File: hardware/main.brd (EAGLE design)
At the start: 99 x 99 mm, 37 parts, among them U1 TMS320F28069_PN_80, U10 TXB0101_DBV_6, U2 TXB0101_DBV_6, U3 TS3A5018_PW_16, U4 TS3A5018_PW_16, U5 SN74LVC4245A_DW_24, U7 Value, U8 Value, U9 SN74LVC4245A_DW_24

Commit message: Finished schematic, laid out board
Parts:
- removed EXTCON2: M10SILK_FEMALE_PTH, SparkFun-Connectors:1X10
- added JP3: M10SILK_FEMALE_PTH, SparkFun-Connectors:1X10
- added U$4, U$8: 8PIN_SOCKET, ControllerCard:CONN-8PIN
- moved C10 78.1 mm to (62.9, 23.6), flipped to the bottom
- moved C11 78.1 mm to (62.9, 19.8), flipped to the bottom
- moved C9 78.1 mm to (62.9, 27.4), flipped to the bottom
- moved C8 72.8 mm to (74.9, 19.3), flipped to the bottom
- moved C6 72.5 mm to (61.9, 10.9), flipped to the bottom
- moved R7 61.6 mm to (77.3, 29.2), turned to 180 degrees
- moved C7 56.5 mm to (52.9, 22.1), flipped to the bottom
- moved R5 55.2 mm to (69.2, 32.9), flipped to the bottom, turned to 270 degrees
- moved C5 49.6 mm to (87.3, 50.4)
- moved U$2 47.0 mm to (52.6, 8.54), turned to 90 degrees
- moved U$5 45.7 mm to (81.3, 51.2), turned to 0 degrees
- moved R2 44.4 mm to (45.4, 8.99)
- moved R3 43.2 mm to (43.7, 4.55), turned to 270 degrees
- moved R1 40.5 mm to (64.7, 3.17)
- moved EXTCON1 40.0 mm to (48.0, 44.4)
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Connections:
- removed net IBUFIN1: U7.23
- removed net IBUFIN2: U7.22
- removed net IBUFIN3: U7.20
- removed net IBUFIN4: U7.19
- removed net IBUFIN5: U7.18
- removed net IBUFIN6: U7.17
- removed net IBUFIN7: U7.15
- removed net IBUFIN8: U7.14
- removed net OBUFIN1: U8.1
- removed net OBUFIN2: U8.3
- removed net OBUFIN3: U8.4
- removed net OBUFIN4: U8.6
- removed net OBUFIN5: U8.7
- removed net OBUFIN6: U8.9
- removed net OBUFIN7: U8.10
- removed net OBUFIN8: U8.12
- new net N$13: U$4.P$1, U8.1
- new net N$14: U$4.P$2, U8.3
- new net N$15: U$4.P$3, U8.4
- new net N$16: U$4.P$4, U8.6
- new net N$17: U$4.P$8, U8.12
- new net N$18: U$4.P$7, U8.10
- new net N$19: U$4.P$6, U8.9
- new net N$20: U$4.P$5, U8.7
- new net N$21: U$8.P$1, U7.23
- new net N$22: U$8.P$2, U7.22
- new net N$23: U$8.P$3, U7.20
- new net N$24: U$8.P$4, U7.19
- new net N$25: U$8.P$8, U7.14
- new net N$26: U$8.P$7, U7.15
- new net N$27: U$8.P$6, U7.17
- new net N$28: U$8.P$5, U7.18
- net !FLASHEN!: now also U1.78; no longer U1.45
- net !FLASHHOLD!: now also U1.80; no longer U1.46
- net !FLASHWP!: now also U1.79; no longer U1.43
- net 3.3V: no longer EXTCON2.1
- net 5V: now also JP3.10
- net BIN1: no longer EXTCON1.4
- net BIN2: no longer EXTCON1.6
- net BIN3: no longer EXTCON1.8
- net BIN4: no longer EXTCON1.10
- net BIN5: no longer EXTCON1.14
- net BIN6: no longer EXTCON1.16
- net BIN7: no longer EXTCON1.18
- net BIN8: no longer EXTCON1.20
- net GND: now also JP3.1; no longer EXTCON2.10
- net IBUFOUT1: now also EXTCON1.4
- net IBUFOUT2: now also EXTCON1.6
- net IBUFOUT3: now also EXTCON1.8
- net IBUFOUT4: now also EXTCON1.10
- net IBUFOUT5: now also EXTCON1.14
- net IBUFOUT6: now also EXTCON1.16
- net IBUFOUT7: now also EXTCON1.18
- net IBUFOUT8: now also EXTCON1.20
- net N$10: now also JP3.8
- net N$11: now also JP3.7
- net N$12: now also JP3.6
- net N$5: now also JP3.2
- net N$6: now also JP3.3
- net N$7: now also JP3.4
- net N$8: now also JP3.5
- net N$9: now also JP3.9
- net SPICLK: now also U1.76; no longer U1.41
- net SPISIMO: now also U1.77; no longer U1.44
- net SPISOMI: now also U1.75; no longer U1.42
- net UCIN1: now also U1.31; no longer U1.8
- net UCIN2: now also U1.32; no longer U1.31
- net UCIN3: now also U1.33; no longer U1.32
- net UCIN4: now also U1.34; no longer U1.33
- net UCIN5: now also U1.35; no longer U1.34
- net UCIN6: now also U1.39; no longer U1.35
- net UCIN7: now also U1.40; no longer U1.39
- net UCIN8: now also U1.41; no longer U1.40
- net UCOUT1: now also U1.42; no longer EXTCON2.2, U1.66
- net UCOUT2: now also U1.43; no longer EXTCON2.3, U1.67
- net UCOUT3: now also U1.44; no longer EXTCON2.4, U1.68
- net UCOUT4: now also U1.45; no longer EXTCON2.5, U1.69
- net UCOUT5: now also U1.46; no longer EXTCON2.6, U1.70
- net UCOUT6: now also U1.52; no longer EXTCON2.7, U1.75
- net UCOUT7: now also U1.53; no longer EXTCON2.8, U1.76
- net UCOUT8: now also U1.59; no longer EXTCON2.9, U1.77
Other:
- board size 99 x 99 mm -> 91 x 58 mm

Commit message: Began routing
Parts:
- moved JP3 26.5 mm to (30.5, 30.5), turned to 180 degrees
- moved C2 14.1 mm to (46.4, 26.0), turned to 270 degrees
- moved EXTCON1 11.2 mm to (58.0, 49.4)
- moved U$3 10.8 mm to (49.6, 24.4), turned to 90 degrees
- moved C1 7.81 mm to (47.9, 18.9)
- moved C7 6.51 mm to (59.4, 21.9), turned to 270 degrees
- moved R1 6.00 mm to (62.3, 8.69), turned to 0 degrees
- moved U5 5.91 mm to (44.9, 38.3), turned to 270 degrees
- moved C6 5.33 mm to (56.6, 11.4), turned to 270 degrees
- moved U3 2.55 mm to (68.2, 36.3)
- moved U10 2.50 mm to (74.7, 33.5)
- moved U8 2.42 mm to (19.9, 19.9), turned to 0 degrees
- moved U$2 1.90 mm to (53.9, 9.96), turned to 270 degrees
- moved U7 1.50 mm to (24.1, 38.2)
- moved C8 1.41 mm to (73.9, 20.3)
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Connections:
- net !FLASHEN!: now also U1.70; no longer U1.78
- net !FLASHHOLD!: now also U1.78; no longer U1.80
- net !FLASHWP!: now also U1.69; no longer U1.79
- net ENEXT: now also U1.7; no longer U1.5
- net RUNSEL: now also U1.5; no longer U1.1
- net USBMON: now also U1.1; no longer U1.60
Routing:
- net USBDP: track 0.00 -> 25.8 mm, vias 0 -> 1
- net USBDM: track 0.00 -> 25.8 mm, vias 0 -> 1
- net UCOUT6: track 0.00 -> 22.9 mm, vias 0 -> 2
- net UCOUT7: track 0.00 -> 22.5 mm, vias 0 -> 2
- net TMS: track 0.00 -> 22.5 mm
- net TCK: track 0.00 -> 22.3 mm
- net TDI: track 0.00 -> 21.9 mm
- net UCOUT8: track 0.00 -> 21.6 mm, vias 0 -> 2
- net TDO: track 0.00 -> 18.9 mm
- net 3.3V: track 0.00 -> 16.7 mm
- net RUNSEL: track 0.00 -> 15.7 mm
- net X1: track 0.00 -> 12.1 mm
- net X2: track 0.00 -> 11.1 mm
- net N$5: track 0.00 -> 10.8 mm
- net RESET: track 0.00 -> 10.6 mm
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
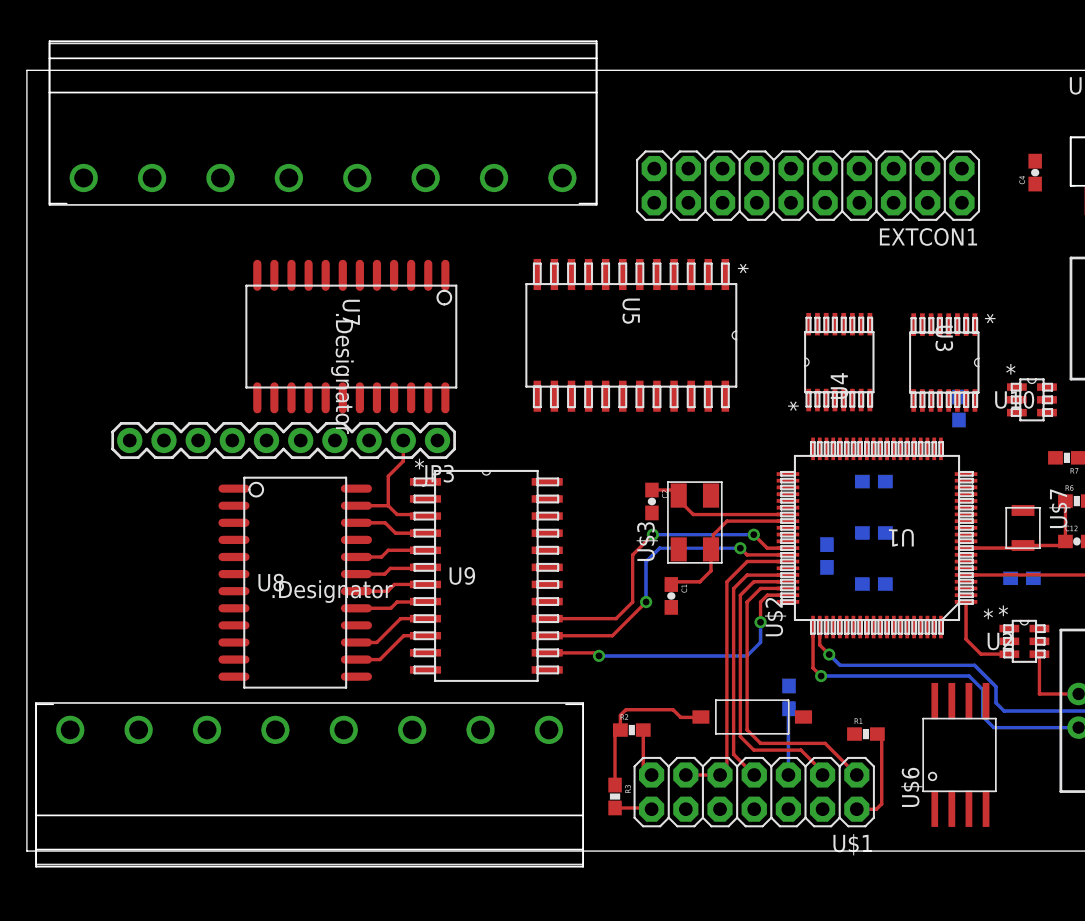
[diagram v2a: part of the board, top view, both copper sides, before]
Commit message: Finished routing SPI Flash and Output section. Re-wired parts of the input section.
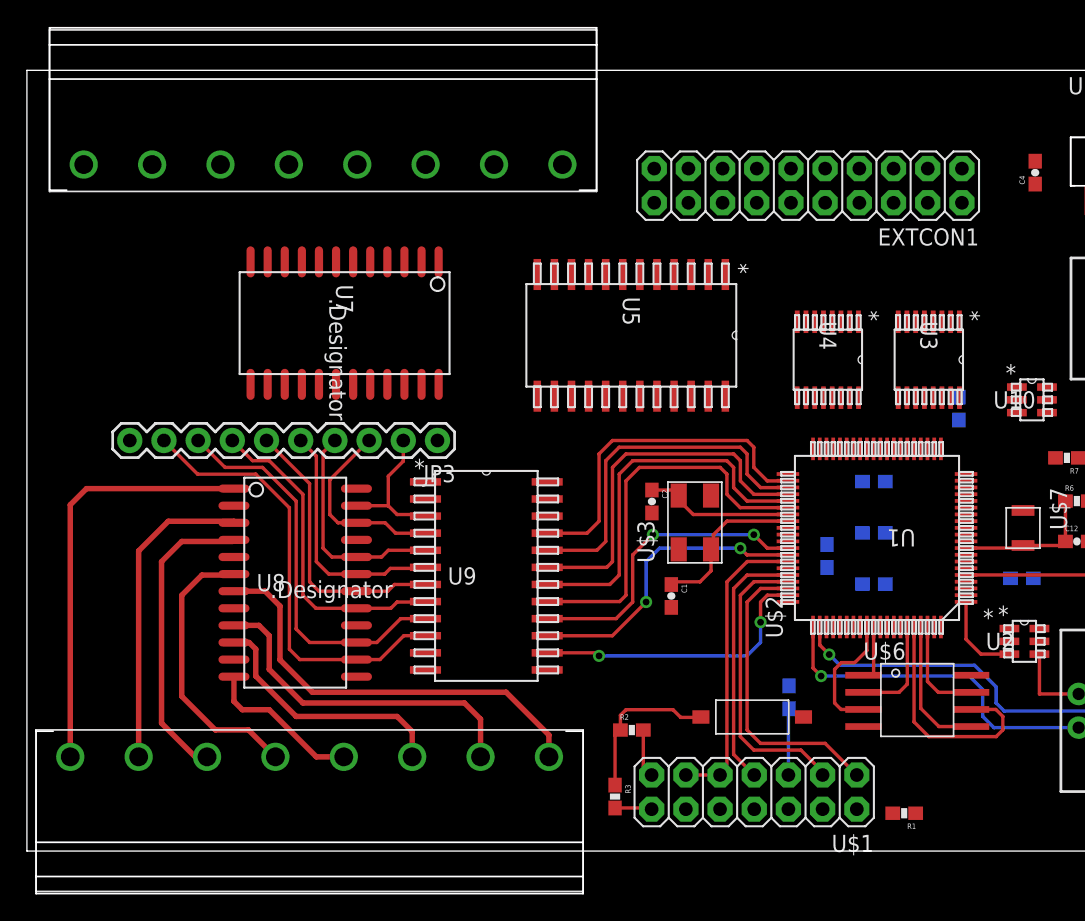
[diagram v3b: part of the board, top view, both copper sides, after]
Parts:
- moved R1 6.53 mm to (65.2, 2.81), turned to 180 degrees
- moved U$6 5.15 mm to (66.1, 11.2), turned to 0 degrees
- moved U$4 2.00 mm to (21.0, 7.00)
- moved U3 1.17 mm to (67.0, 36.5)
- moved U7 1.12 mm to (23.6, 39.2)
- moved U$8 1.00 mm to (22.0, 51.0)
- moved U4 0.87 mm to (59.5, 36.5), turned to 270 degrees
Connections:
- net N$17: now also U$4.P$5; no longer U$4.P$8
- net N$18: now also U$4.P$6; no longer U$4.P$7
- net N$19: now also U$4.P$7; no longer U$4.P$6
- net N$20: now also U$4.P$8; no longer U$4.P$5
- net UCIN1: now also U1.33; no longer U1.31
- net UCIN2: now also U1.34; no longer U1.32
- net UCIN3: now also U1.32; no longer U1.33
- net UCIN4: now also U1.31; no longer U1.34
- net UCIN7: now also U1.41; no longer U1.40
- net UCIN8: now also U1.40; no longer U1.41
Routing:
- net N$20: track 0.00 -> 31.8 mm
- net N$13: track 0.00 -> 31.4 mm
- net UCOUT5: track 0.00 -> 29.1 mm
- net UCOUT4: track 0.00 -> 28.2 mm
- net UCOUT3: track 0.00 -> 27.6 mm
- net N$9: track 5.87 -> 33.1 mm
- net UCOUT2: track 0.00 -> 26.7 mm
- net UCOUT1: track 0.00 -> 25.8 mm
- net N$19: track 0.00 -> 25.5 mm
- net N$10: track 5.86 -> 29.4 mm
- net N$14: track 0.00 -> 23.4 mm
- net N$15: track 0.00 -> 22.5 mm
- net N$16: track 0.00 -> 20.9 mm
- net N$18: track 0.00 -> 19.0 mm
- net N$11: track 5.34 -> 24.1 mm
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
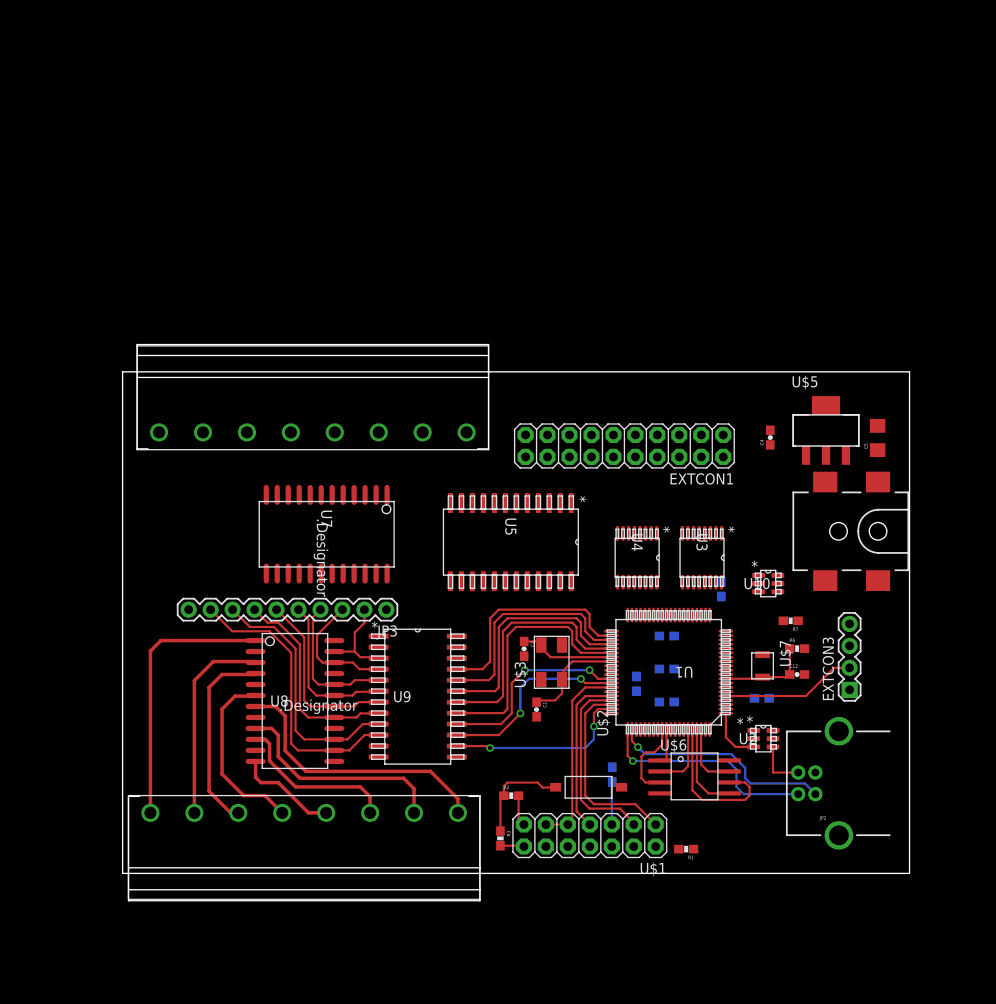
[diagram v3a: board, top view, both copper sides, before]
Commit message: Updated input ribbon connector schematic, began to route input analog switches
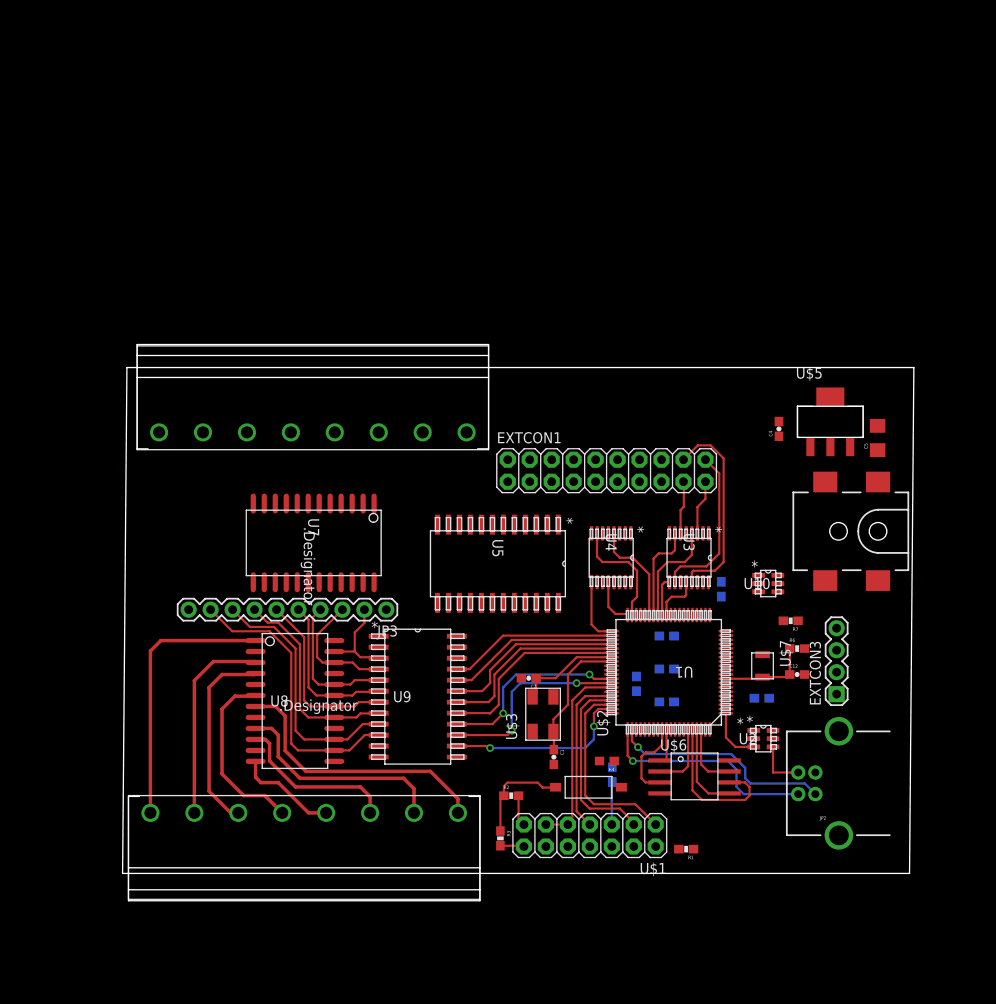
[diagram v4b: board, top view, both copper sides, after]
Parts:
- added R4: 1.5KOHM, SparkFun-Resistors:0603
- moved U$3 6.08 mm to (48.6, 18.4)
- moved C1 5.85 mm to (49.9, 13.4)
- moved EXTCON1 3.52 mm to (56.0, 46.6), turned to 0 degrees
- moved C2 3.44 mm to (47.0, 22.6), turned to 180 degrees
- moved U4 3.00 mm to (56.5, 36.5)
- moved U5 2.92 mm to (43.4, 35.8)
- moved U7 1.80 mm to (22.1, 38.2)
- moved EXTCON3 1.58 mm to (82.6, 20.7)
- moved U3 1.50 mm to (65.5, 36.5)
- moved C4 1.41 mm to (75.9, 51.4)
- moved U$5 1.12 mm to (81.8, 52.2)
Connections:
- net 3.3V: now also R4.2
- net IBUFOUT1: now also EXTCON1.9; no longer EXTCON1.4
- net IBUFOUT2: now also EXTCON1.7; no longer EXTCON1.6
- net IBUFOUT3: now also EXTCON1.5; no longer EXTCON1.8
- net IBUFOUT4: now also EXTCON1.3; no longer EXTCON1.10
- net IBUFOUT5: now also EXTCON1.10; no longer EXTCON1.14
- net IBUFOUT6: now also EXTCON1.8; no longer EXTCON1.16
- net IBUFOUT7: now also EXTCON1.6; no longer EXTCON1.18
- net IBUFOUT8: now also EXTCON1.4; no longer EXTCON1.20
- net SW1: now also EXTCON1.19; no longer EXTCON1.3
- net SW2: now also EXTCON1.17; no longer EXTCON1.5
- net SW3: now also EXTCON1.20; no longer EXTCON1.7
- net SW4: now also EXTCON1.18; no longer EXTCON1.9
- net SW5: now also EXTCON1.15; no longer EXTCON1.13
- net SW6: now also EXTCON1.13; no longer EXTCON1.15
- net SW7: now also EXTCON1.16; no longer EXTCON1.17
- net SW8: now also EXTCON1.14; no longer EXTCON1.19
- net USBDP: now also R4.1
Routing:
- net SW4: track 0.00 -> 23.3 mm
- net SW3: track 0.00 -> 18.7 mm
- net RUNSEL: track 15.7 -> 0.00 mm
- net UCIN6: track 0.00 -> 13.4 mm
- net UCIN1: track 0.00 -> 12.2 mm
- net UCIN5: track 0.00 -> 12.0 mm
- net UCIN2: track 0.00 -> 11.3 mm
- net UCIN7: track 0.00 -> 7.54 mm
- net UCOUT2: track 26.7 -> 19.8 mm
- net UCOUT3: track 27.6 -> 21.0 mm
- net UCOUT5: track 29.1 -> 22.6 mm
- net SW1: track 0.00 -> 6.36 mm
- net UCOUT4: track 28.2 -> 21.9 mm
- net UCOUT1: track 25.8 -> 19.5 mm
- net SW2: track 0.00 -> 6.15 mm
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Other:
- board size 91 x 58 mm -> 91.5 x 58.5 mm
